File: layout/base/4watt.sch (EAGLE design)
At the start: 45 parts, among them IC2 FT232RL, Q1 IRF7413, Q2 IRF7413, Q3 IRF7413, Q4 IRF7413, T1 BC848, T2 BC848, T3 BC848, T4 BC848, T5 BC848, T6 BC848, U1 MOD-WIFI-ESP8266-DEV_SMD

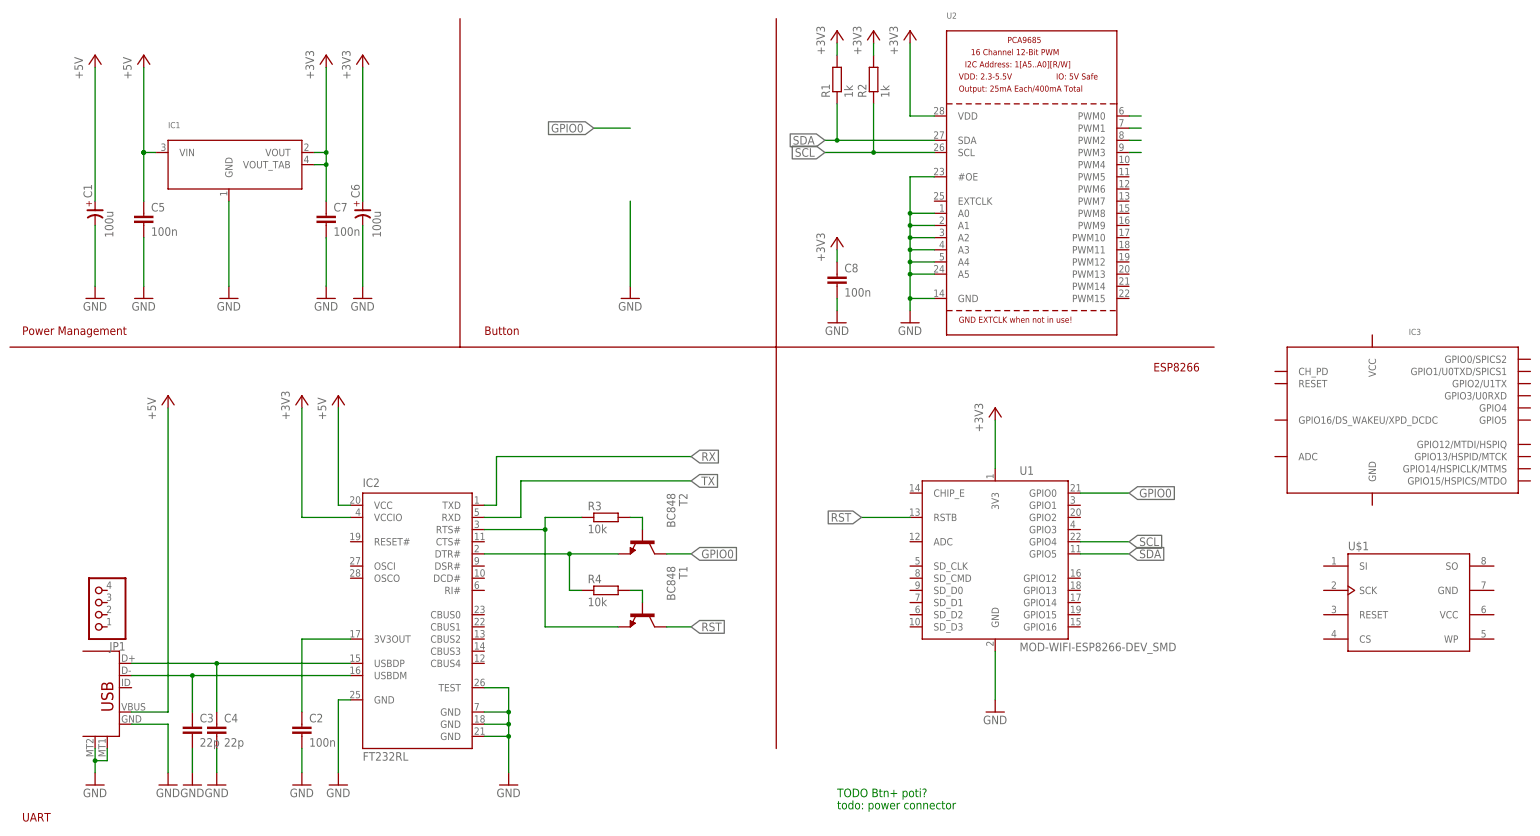
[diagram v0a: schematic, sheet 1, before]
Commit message: new pinout
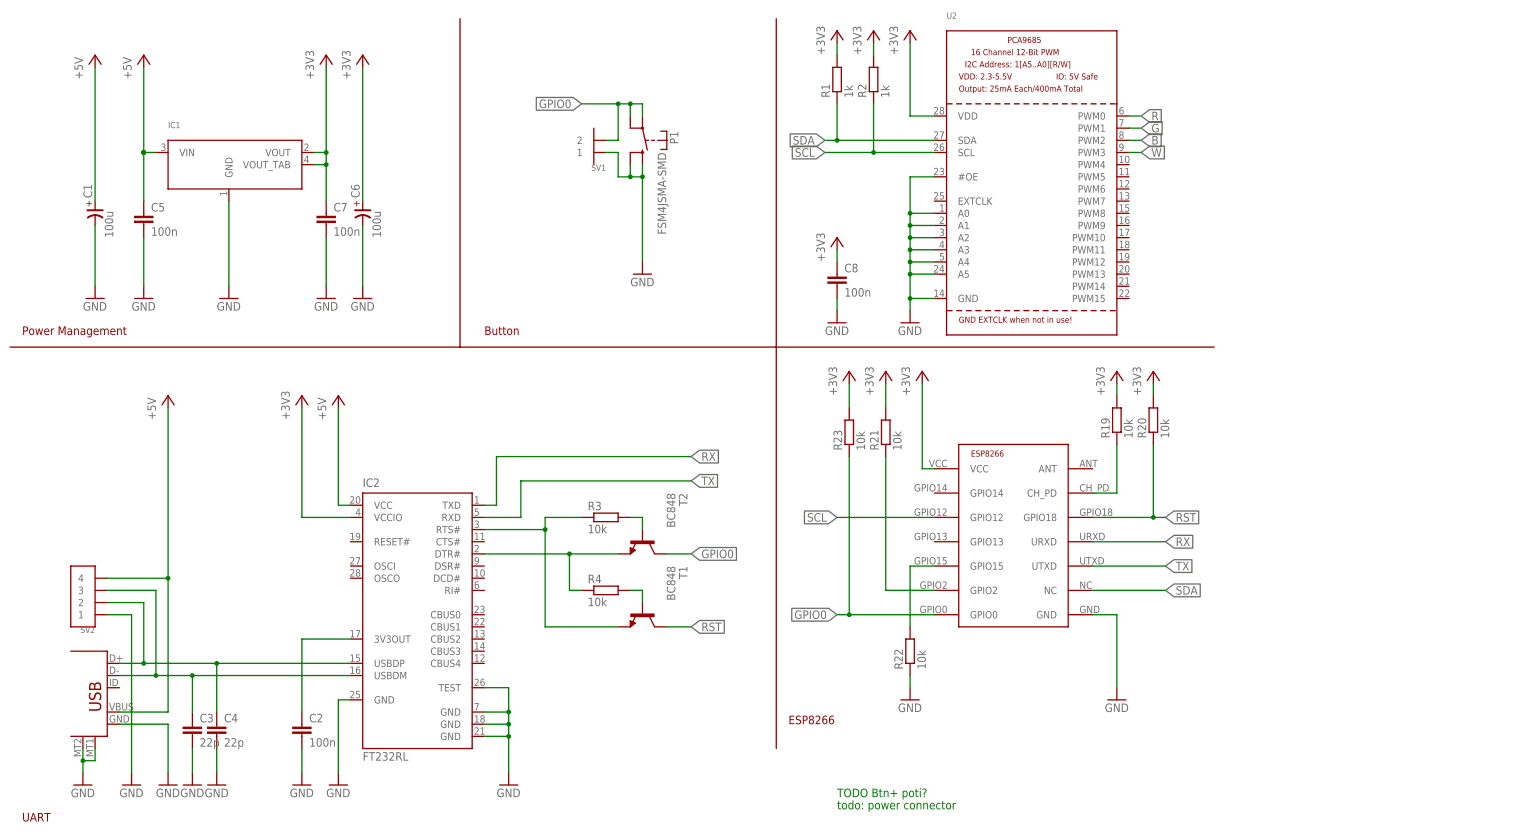
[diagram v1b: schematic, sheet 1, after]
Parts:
- removed IC3: (no value), ESP8266-2:ESP-12
- removed JP1: (no value), pinhead-2:PINHD-1X04_2.54
- removed U$1: DUMMY, SparkFun:ATMEL_DATA_FLASH
- removed U1: MOD-WIFI-ESP8266-DEV_SMD, ESP8266 2:MOD-WIFI-ESP8266-DEV_SMD
- added P1: FSM4JSMA-SMD, switch-misc:FSM4JSMA-SMD
- added R19, R20, R21, R22, R23: 10k, rcl-2:R-EU_R0603
- added SV1: 1X2SMD-2.54LIEGEND, sid:1X2SMD-2.54LIEGEND
- added SV2: 1X4SMD-2.54LIEGEND, sid:1X4SMD-2.54LIEGEND
- added U$2: ESP8266, ESP8266:ESP8266
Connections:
- new net GPIO15: R22.2, U$2.GPIO15
- new net N$2: R19.1, U$2.CH_PD
- new net N$6: R21.1, U$2.GPIO2
- net +3V3: now also R19.2, R20.2, R21.2, R23.2, U$2.VCC; no longer U1.3V3
- net +5V: now also SV2.4
- net GND: now also P1.S, P1.S@1, R22.1, SV1.1, SV2.1, U$2.GND; no longer U1.GND
- net GPIO0: now also P1.P, P1.P@1, R23.1, SV1.2, U$2.GPIO0; no longer U1.GPIO0
- net N$3: now also SV2.2
- net N$4: now also SV2.3
- net RST: now also R20.1, U$2.GPIO18; no longer U1.RSTB
- net RX: now also U$2.URXD
- net SCL: now also U$2.GPIO12; no longer U1.GPIO4
- net SDA: now also U$2.NC; no longer U1.GPIO5
- net TX: now also U$2.UTXD

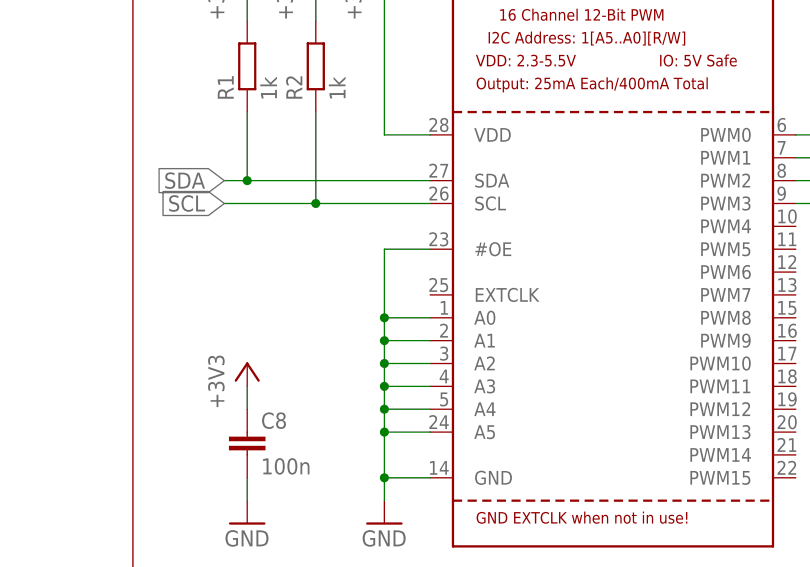
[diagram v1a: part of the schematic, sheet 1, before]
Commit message: extclk to gnd
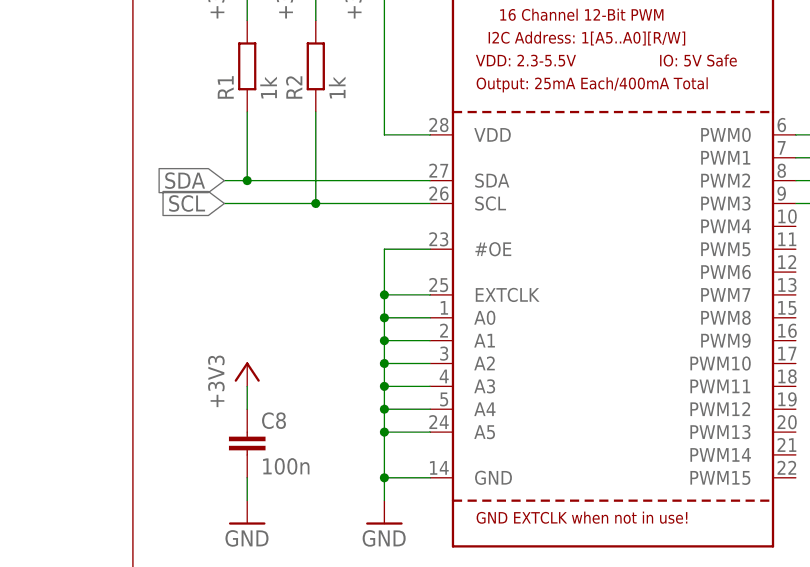
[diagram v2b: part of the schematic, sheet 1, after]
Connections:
- net GND: now also U2.EXTCLK
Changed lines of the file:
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@@
 <pinref part="U2" gate="G$1" pin="#OE"/>
 <wire x1="198.12" y1="142.24" x2="193.04" y2="142.24" width="0.1524" layer="91"/>
-<wire x1="193.04" y1="142.24" x2="193.04" y2="134.62" width="0.1524" layer="91"/>
+<wire x1="193.04" y1="142.24" x2="193.04" y2="137.16" width="0.1524" layer="91"/>
+<pinref part="U2" gate="G$1" pin="EXTCLK"/>
+<wire x1="193.04" y1="137.16" x2="193.04" y2="134.62" width="0.1524" layer="91"/>
+<wire x1="198.12" y1="137.16" x2="193.04" y2="137.16" width="0.1524" layer="91"/>
+<junction x="193.04" y="137.16"/>
 </segment>
 <segment>

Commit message: 4watt done
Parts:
- added C9: 100n, rcl:C-EUC0603
- R10, R11, R12, R16, R17, R5, R6, R7, R8, R9: value 3,3-3,9 -> 3R6
- R13, R14, R15, R18: value 1k5 -> 360
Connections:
- net GND: now also C9.2
- net RST: now also C9.1
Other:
- note added: "3.0V"
- note removed: "TODO Btn+ poti?"
- note removed: "todo: power connector"
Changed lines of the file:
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@@
 <part name="T4" library="transistor" deviceset="BC848" device=""/>
 <part name="T5" library="transistor" deviceset="BC848" device=""/>
-<part name="R8" library="rcl-2" deviceset="R-EU_" device="M1206" value="3,3-3,9"/>
-<part name="R9" library="rcl-2" deviceset="R-EU_" device="M1206" value="3,3-3,9"/>
-<part name="R6" library="rcl-2" deviceset="R-EU_" device="M1206" value="3,3-3,9"/>
-<part name="R7" library="rcl-2" deviceset="R-EU_" device="M1206" value="3,3-3,9"/>
-<part name="R10" library="rcl-2" deviceset="R-EU_" device="M1206" value="3,3-3,9"/>
-<part name="R11" library="rcl-2" deviceset="R-EU_" device="M1206" value="3,3-3,9"/>
-<part name="R5" library="rcl-2" deviceset="R-EU_" device="M1206" value="3,3-3,9"/>
-<part name="R12" library="rcl-2" deviceset="R-EU_" device="M1206" value="3,3-3,9"/>
-<part name="R13" library="rcl-2" deviceset="R-EU_" device="R0603" value="1k5"/>
-<part name="R14" library="rcl-2" deviceset="R-EU_" device="R0603" value="1k5"/>
-<part name="R15" library="rcl-2" deviceset="R-EU_" device="R0603" value="1k5"/>
+<part name="R8" library="rcl-2" deviceset="R-EU_" device="M1206" value="3R6"/>
+<part name="R9" library="rcl-2" deviceset="R-EU_" device="M1206" value="3R6"/>
+<part name="R6" library="rcl-2" deviceset="R-EU_" device="M1206" value="3R6"/>
+<part name="R7" library="rcl-2" deviceset="R-EU_" device="M1206" value="3R6"/>
+<part name="R10" library="rcl-2" deviceset="R-EU_" device="M1206" value="3R6"/>
+<part name="R11" library="rcl-2" deviceset="R-EU_" device="M1206" value="3R6"/>
+<part name="R5" library="rcl-2" deviceset="R-EU_" device="M1206" value="3R6"/>
+<part name="R12" library="rcl-2" deviceset="R-EU_" device="M1206" value="3R6"/>
+<part name="R13" library="rcl-2" deviceset="R-EU_" device="R0603" value="360"/>
+<part name="R14" library="rcl-2" deviceset="R-EU_" device="R0603" value="360"/>
+<part name="R15" library="rcl-2" deviceset="R-EU_" device="R0603" value="360"/>
 <part name="GND14" library="supply1" deviceset="GND" device=""/>
 <part name="GND17" library="supply1" deviceset="GND" device=""/>
@@
 <part name="Q4" library="transistor-fet" deviceset="IRF7413" device=""/>
 <part name="T6" library="transistor" deviceset="BC848" device=""/>
-<part name="R16" library="rcl-2" deviceset="R-EU_" device="M1206" value="3,3-3,9"/>
-<part name="R17" library="rcl-2" deviceset="R-EU_" device="M1206" value="3,3-3,9"/>
-<part name="R18" library="rcl-2" deviceset="R-EU_" device="R0603" value="1k5"/>
+<part name="R16" library="rcl-2" deviceset="R-EU_" device="M1206" value="3R6"/>
+<part name="R17" library="rcl-2" deviceset="R-EU_" device="M1206" value="3R6"/>
+<part name="R18" library="rcl-2" deviceset="R-EU_" device="R0603" value="360"/>
 <part name="GND16" library="supply1" deviceset="GND" device=""/>
 <part name="GND19" library="supply1" deviceset="GND" device=""/>
@@
 <part name="SV2" library="sid" deviceset="1X4SMD-2.54LIEGEND" device=""/>
 <part name="GND30" library="supply1" deviceset="GND" device=""/>
+<part name="C9" library="rcl" deviceset="C-EU" device="C0603" value="100n"/>
+<part name="GND31" library="supply1" deviceset="GND" device=""/>
 </parts>
 <sheets>
@@
 <text x="7.62" y="7.62" size="1.778" layer="94">UART</text>
 <text x="167.64" y="27.94" size="1.778" layer="94">ESP8266</text>
-<text x="177.8" y="12.7" size="1.778" layer="91">TODO Btn+ poti?</text>
-<text x="177.8" y="10.16" size="1.778" layer="91">todo: power connector</text>
 </plain>
 <instances>
@@
 <instance part="SV2" gate="G$1" x="22.86" y="53.34" rot="R180"/>
 <instance part="GND30" gate="1" x="30.48" y="15.24"/>
+<instance part="C9" gate="G$1" x="243.84" y="45.72"/>
+<instance part="GND31" gate="1" x="243.84" y="33.02"/>
 </instances>
 <busses>
@@
 <wire x1="30.48" y1="50.8" x2="30.48" y2="17.78" width="0.1524" layer="91"/>
 </segment>
+<segment>
+<pinref part="C9" gate="G$1" pin="2"/>
+<pinref part="GND31" gate="1" pin="GND"/>
+<wire x1="243.84" y1="35.56" x2="243.84" y2="40.64" width="0.1524" layer="91"/>
+</segment>
 </net>
 <net name="N$12" class="0">
@@
 <wire x1="243.84" y1="71.12" x2="243.84" y2="86.36" width="0.1524" layer="91"/>
 <junction x="243.84" y="71.12"/>
+<pinref part="C9" gate="G$1" pin="1"/>
+<wire x1="243.84" y1="71.12" x2="243.84" y2="48.26" width="0.1524" layer="91"/>
 </segment>
 </net>
@@
 <sheet>
 <plain>
+<text x="30.48" y="86.36" size="1.778" layer="94">3.0V</text>
+<text x="93.98" y="86.36" size="1.778" layer="94">3.0V</text>
+<text x="154.94" y="86.36" size="1.778" layer="94">3.0V</text>
+<text x="215.9" y="86.36" size="1.778" layer="94">3.0V</text>
 </plain>
 <instances>
